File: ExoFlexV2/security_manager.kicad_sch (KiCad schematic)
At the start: 0 parts

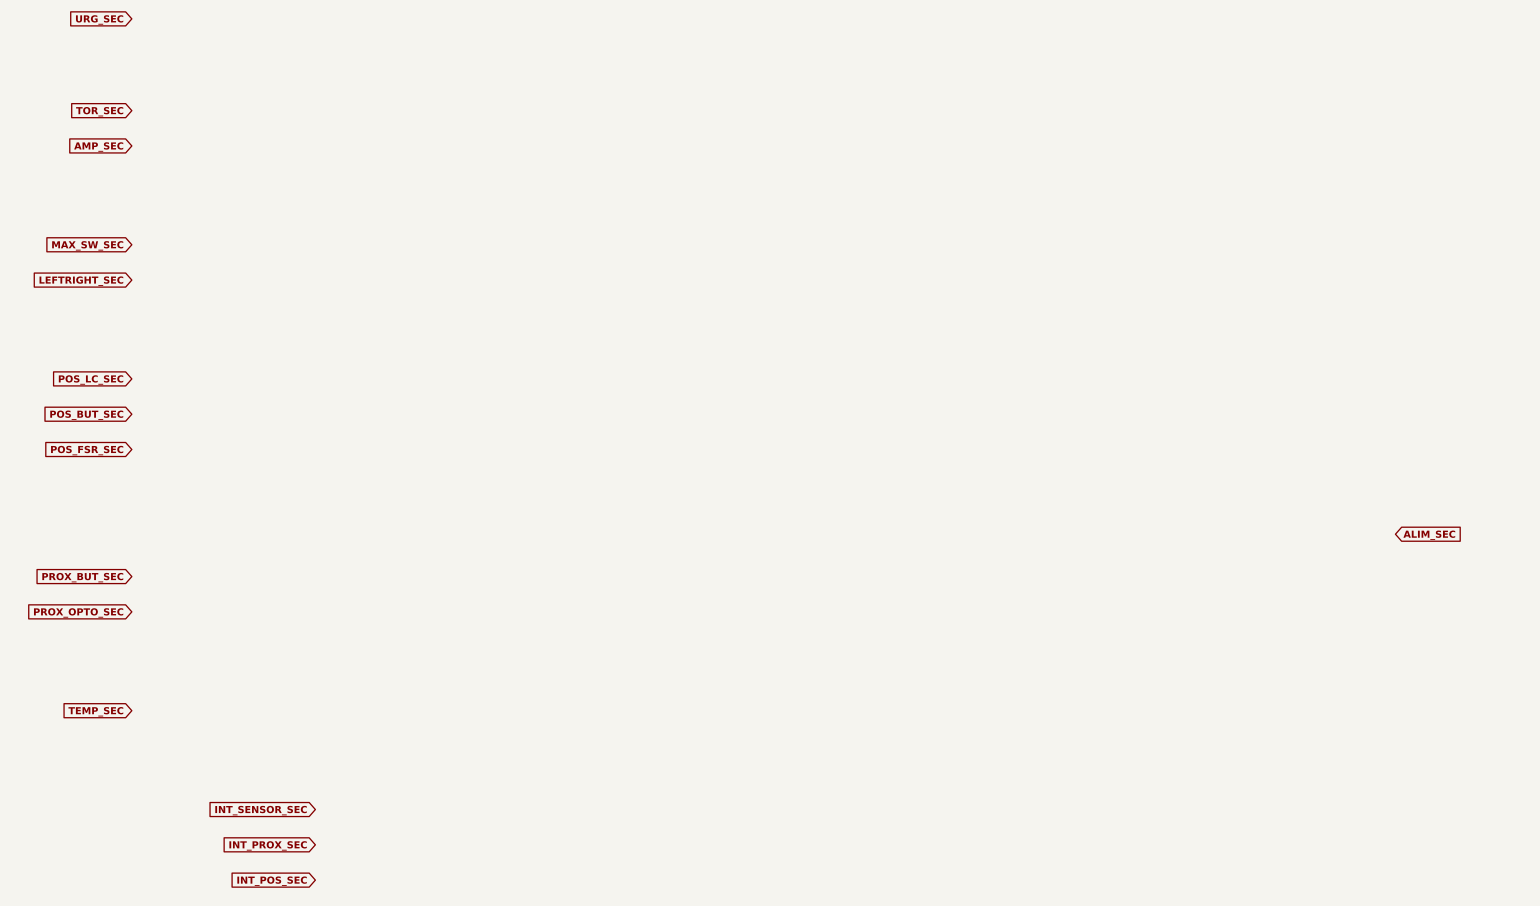
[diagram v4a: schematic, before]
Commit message: Mise à jour signaux STM
- Condo de découplage
- Signaux supplémentaire pour le STM
- Page GND sera pour Multiplexeur
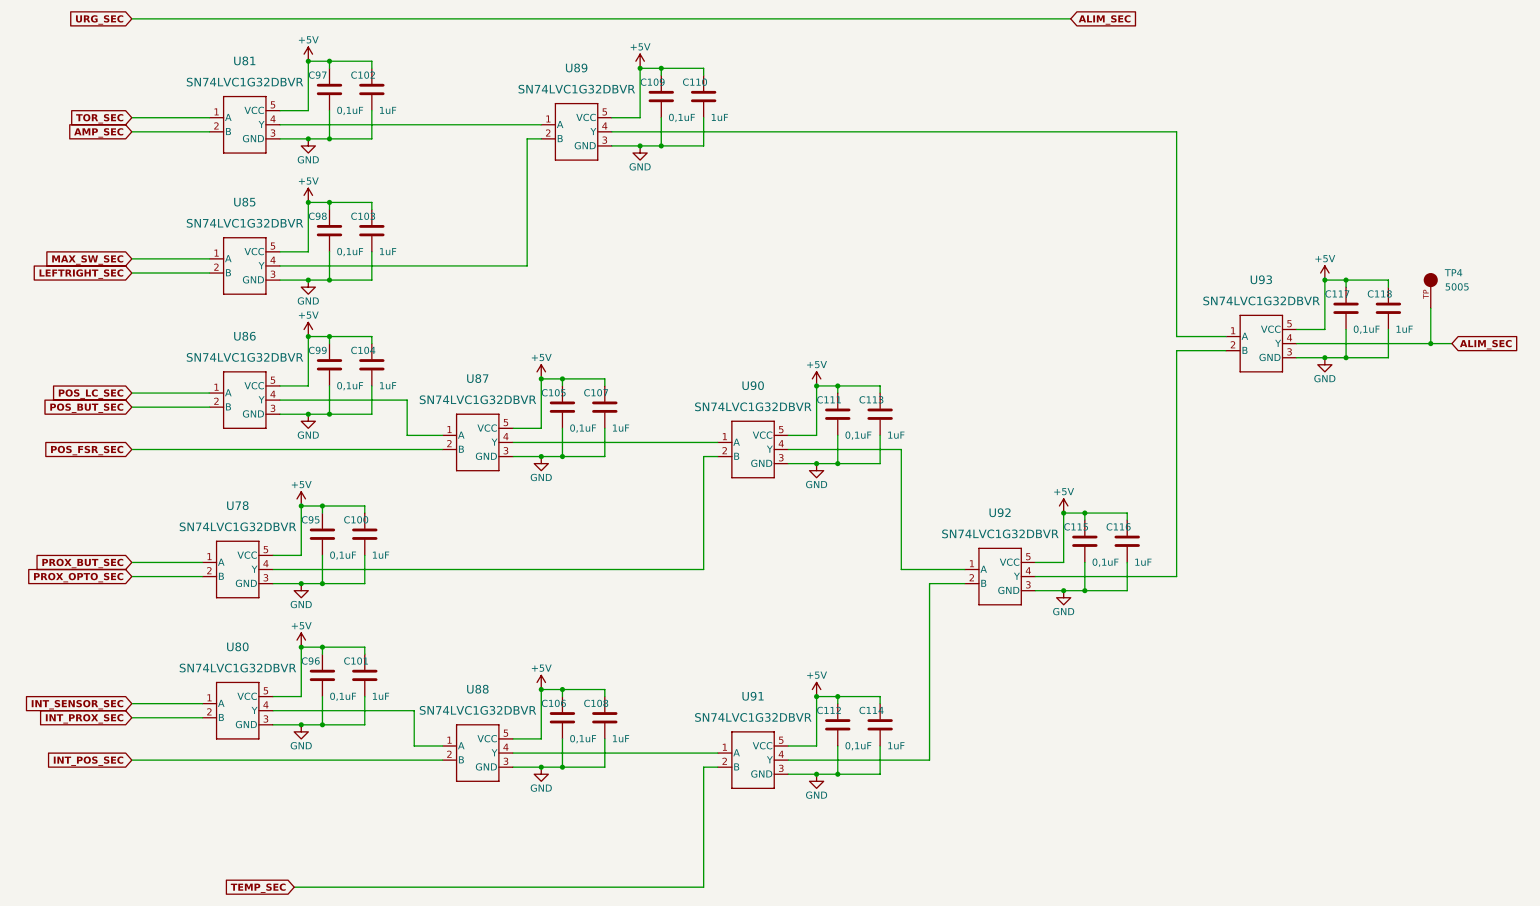
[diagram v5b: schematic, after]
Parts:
- added C100, C101, C102, C103, C104, C107, C108, C110, C113, C114, C116, C118: 1uF, Capacitor_SMD:C_0603_1608Metric, symbol Device:C
- added C105, C106, C109, C111, C112, C115, C117, C95, C96, C97, C98, C99: 0,1uF, Capacitor_SMD:C_0603_1608Metric, symbol Device:C
- added TP4: 5005, FootPrint:KEYSTONE_5005, symbol SymLib:5005
- added U78, U80, U81, U85, U86, U87, U88, U89, U90, U91, U92, U93: SN74LVC1G32DBVR, FootPrint:SOT95P270X145-5N, symbol SymLib:SN74LVC1G32DBVR
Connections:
- net ALIM_SEC: now also TP4.TP, U93.4 (Y)
- net AMP_SEC: now also U81.2 (B)
- net INT_POS_SEC: now also U88.2 (B)
- net INT_PROX_SEC: now also U80.2 (B)
- net INT_SENSOR_SEC: now also U80.1 (A)
- net LEFTRIGHT_SEC: now also U85.2 (B)
- net MAX_SW_SEC: now also U85.1 (A)
- net POS_BUT_SEC: now also U86.2 (B)
- net POS_FSR_SEC: now also U87.2 (B)
- net POS_LC_SEC: now also U86.1 (A)
- net PROX_BUT_SEC: now also U78.1 (A)
- net PROX_OPTO_SEC: now also U78.2 (B)
- net TEMP_SEC: now also U91.2 (B)
- net TOR_SEC: now also U81.1 (A)
- new net: U90.4 (Y), U92.1 (A)
- new net: U91.4 (Y), U92.2 (B)
- new net: U92.4 (Y), U93.2 (B)
- new net: U87.4 (Y), U90.1 (A)
- new net: U78.4 (Y), U90.2 (B)
- new net: U86.4 (Y), U87.1 (A)
- new net: U88.4 (Y), U91.1 (A)
- new net: U81.4 (Y), U89.1 (A)
- new net: U85.4 (Y), U89.2 (B)
- new net: U89.4 (Y), U93.1 (A)
- new net: U80.4 (Y), U88.1 (A)
- new net +5V: C100.1, C101.1, C102.1, C103.1, C104.1, C105.1, C106.1, C107.1, C108.1, C109.1, C110.1, C111.1, C112.1, C113.1, C114.1, C115.1, C116.1, C117.1, C118.1, C95.1, C96.1, C97.1, C98.1, C99.1, U78.5 (VCC), U80.5 (VCC), U81.5 (VCC), U85.5 (VCC), U86.5 (VCC), U87.5 (VCC), U88.5 (VCC), U89.5 (VCC), U90.5 (VCC), U91.5 (VCC), U92.5 (VCC), U93.5 (VCC)
- new net GND: C100.2, C101.2, C102.2, C103.2, C104.2, C105.2, C106.2, C107.2, C108.2, C109.2, C110.2, C111.2, C112.2, C113.2, C114.2, C115.2, C116.2, C117.2, C118.2, C95.2, C96.2, C97.2, C98.2, C99.2, U78.3 (GND), U80.3 (GND), U81.3 (GND), U85.3 (GND), U86.3 (GND), U87.3 (GND), U88.3 (GND), U89.3 (GND), U90.3 (GND), U91.3 (GND), U92.3 (GND), U93.3 (GND)

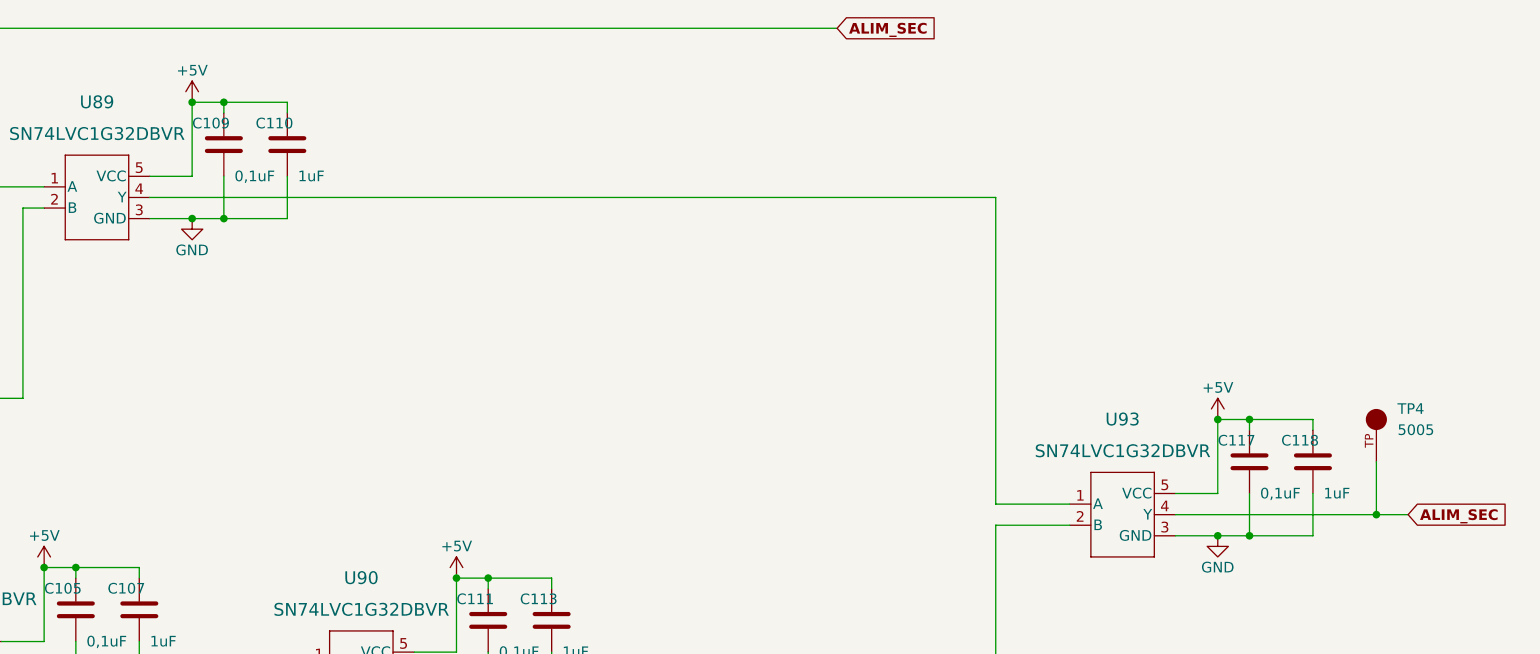
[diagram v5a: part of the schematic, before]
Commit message: Finalisation 1
- Ajout de pages pour la gestion des signaux négatif
- Modification des pages de torque et amplitude
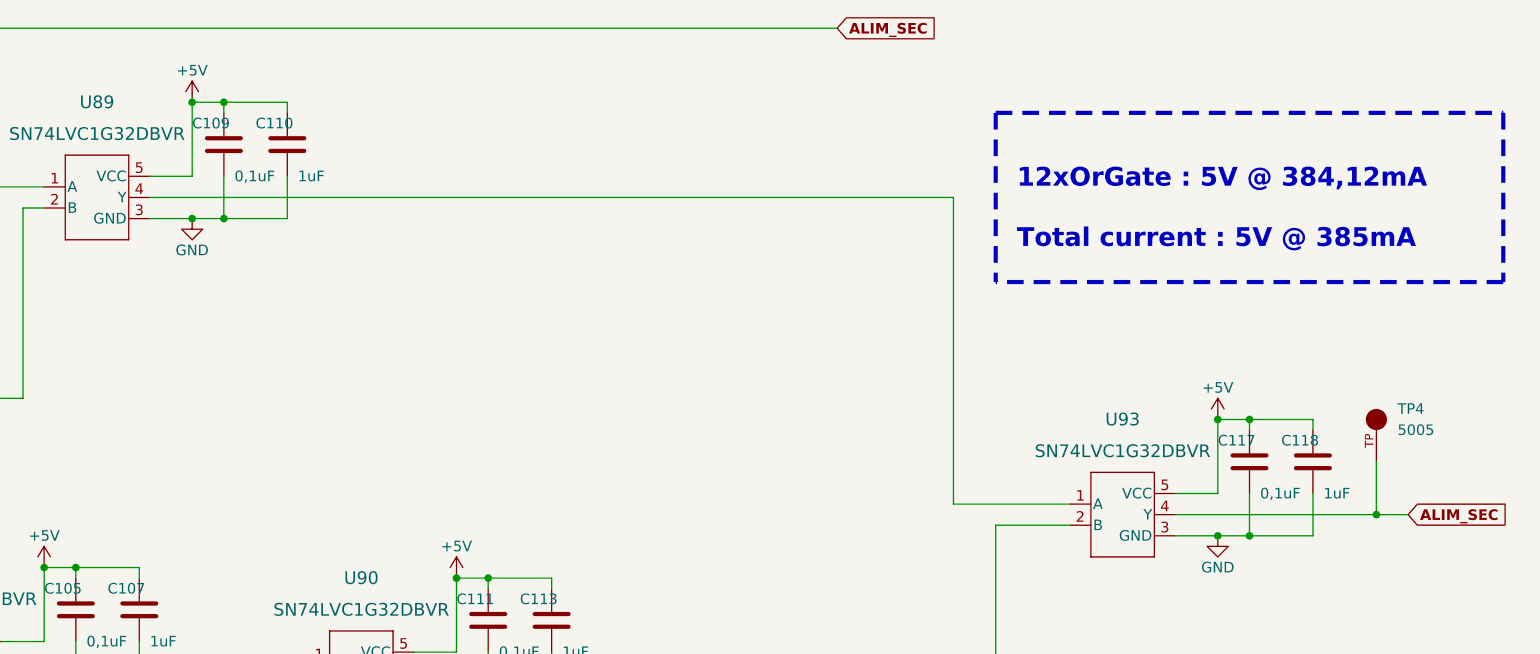
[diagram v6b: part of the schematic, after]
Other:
- note added: "12xOrGate : 5V @ 384,12mA Total current : 5V @ 385mA"
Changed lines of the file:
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@@
     (stroke (width 0) (type default) (color 0 0 0 0))
   )
-  (wire (pts (xy 222.25 41.91) (xy 222.25 78.74))
-    (stroke (width 0) (type default) (color 0 0 0 0))
+  (wire (pts (xy 217.17 41.91) (xy 217.17 78.74))
+    (stroke (width 0) (type default) (color 0 0 0 0))
+  )
+  (polyline (pts (xy 222.25 31.75) (xy 222.25 52.07))
+    (stroke (width 0.5) (type dash) (color 255 148 44 1))
   )
   (wire (pts (xy 68.58 110.49) (xy 68.58 109.22))
@@
     (stroke (width 0) (type default) (color 0 0 0 0))
   )
+  (polyline (pts (xy 283.21 52.07) (xy 222.25 52.07))
+    (stroke (width 0.5) (type dash) (color 255 148 44 1))
+  )
   (wire (pts (xy 66.04 54.61) (xy 69.85 54.61))
     (stroke (width 0) (type default) (color 0 0 0 0))
@@
     (stroke (width 0) (type default) (color 0 0 0 0))
   )
-  (wire (pts (xy 222.25 78.74) (xy 231.14 78.74))
+  (wire (pts (xy 217.17 78.74) (xy 231.14 78.74))
     (stroke (width 0) (type default) (color 0 0 0 0))
   )
@@
     (stroke (width 0) (type default) (color 0 0 0 0))
   )
+  (polyline (pts (xy 222.25 31.75) (xy 283.21 31.75))
+    (stroke (width 0.5) (type dash) (color 255 148 44 1))
+  )
   (wire (pts (xy 111.76 143.51) (xy 111.76 142.24))
     (stroke (width 0) (type default) (color 0 0 0 0))
@@
     (stroke (width 0) (type default) (color 0 0 0 0))
   )
-  (wire (pts (xy 120.65 41.91) (xy 222.25 41.91))
+  (wire (pts (xy 120.65 41.91) (xy 217.17 41.91))
     (stroke (width 0) (type default) (color 0 0 0 0))
   )
@@
     (stroke (width 0) (type default) (color 0 0 0 0))
   )
+  (polyline (pts (xy 283.21 31.75) (xy 283.21 52.07))
+    (stroke (width 0.5) (type dash) (color 255 148 44 1))
+  )
   (wire (pts (xy 213.36 119.38) (xy 213.36 124.46))
     (stroke (width 0) (type default) (color 0 0 0 0))
@@
     (stroke (width 0) (type default) (color 0 0 0 0))
   )
+  (text "12xOrGate : 5V @ 384,12mA\n\nTotal current : 5V @ 385mA"
+    (at 224.79 48.26 0)
+    (effects (font (size 2.25 2.25) (thickness 0.5) bold) (justify left bottom))
+  )
   (global_label "PROX_BUT_SEC" (shape input) (at 34.29 119.38 180) (fields_autoplaced)
